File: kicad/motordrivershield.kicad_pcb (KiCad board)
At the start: 2 copper layers, 100 x 60 mm, 142 parts, among them CN1 ARDUINO_MKR, CN2 QWIIC, P1 CONN_01X03, P2 CONN_01X03, P5 WR-TBL_691313710002, P6 WR-TBL_691313710002, P7 CONN_01X02, P8 WR-TBL_691313710002, Q1 2N7002, U1 PCA9685_TSSOP28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

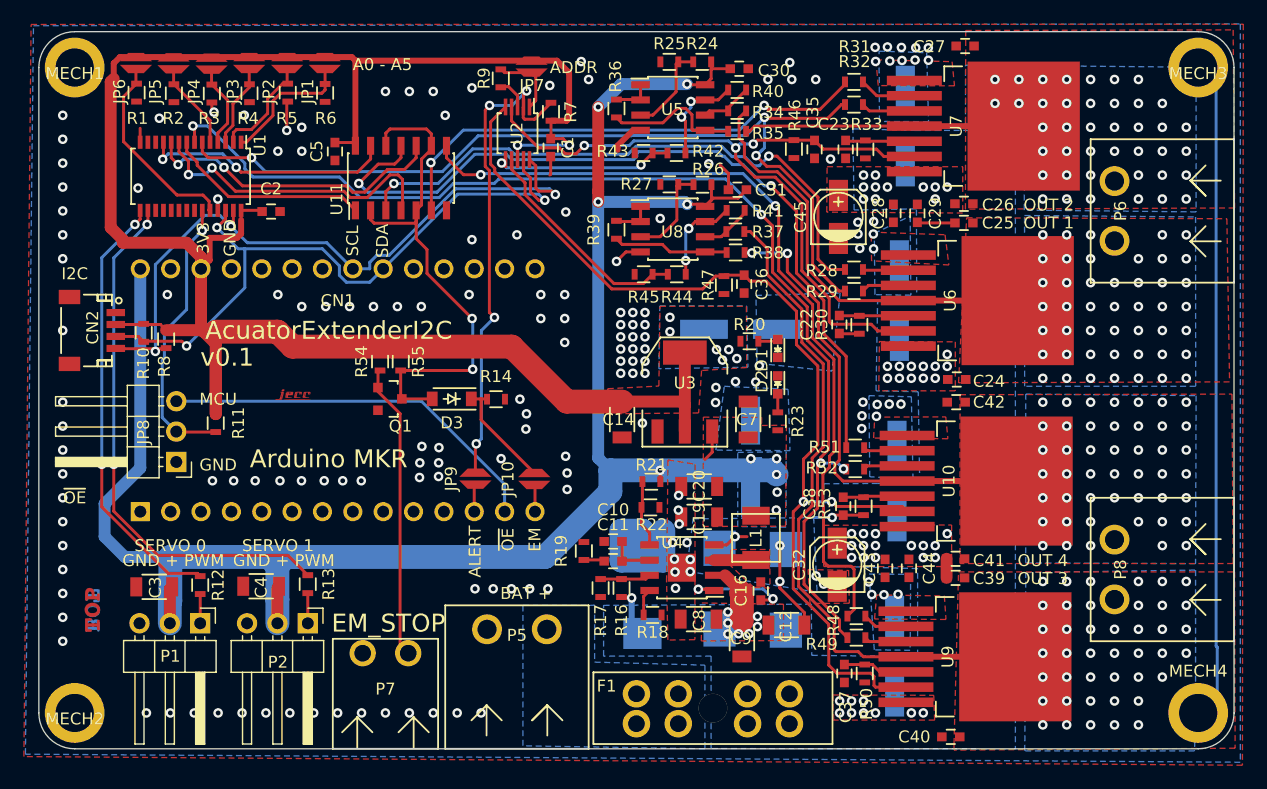
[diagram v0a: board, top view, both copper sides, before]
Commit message: added nano footprint
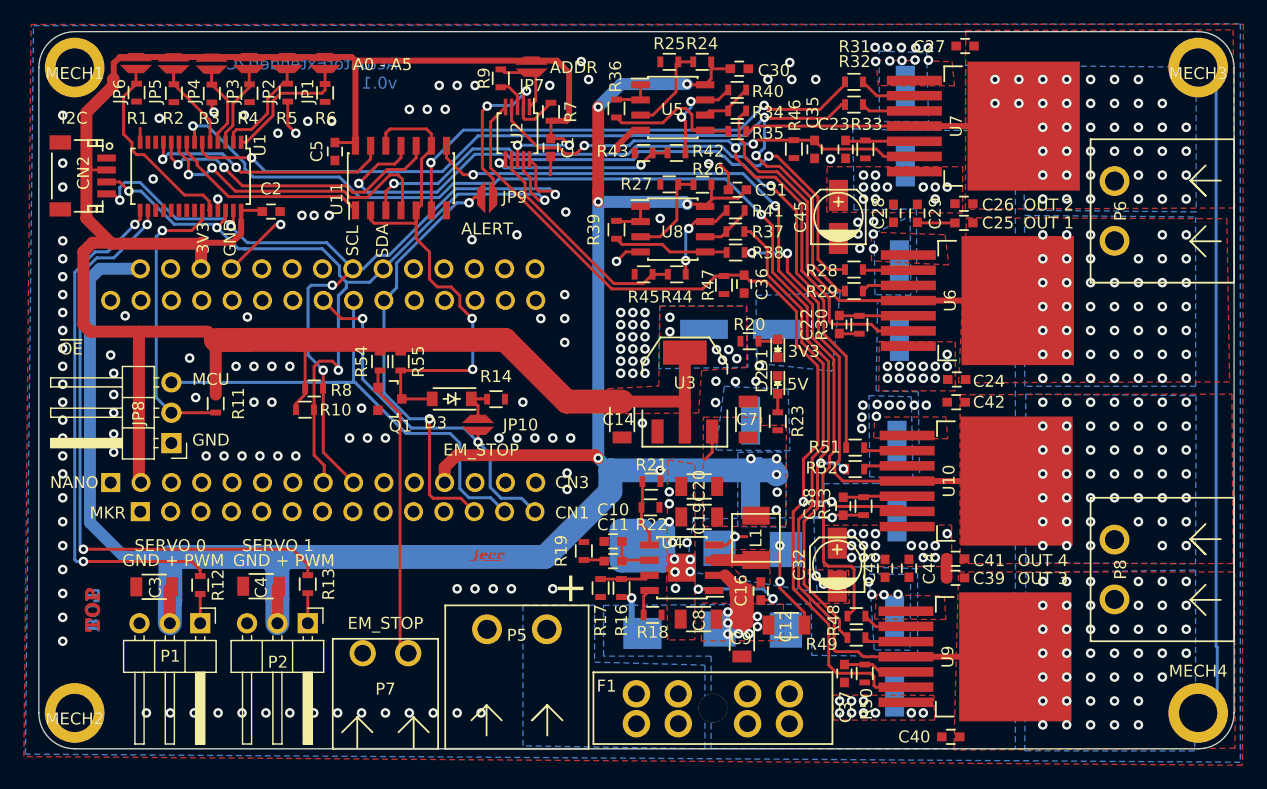
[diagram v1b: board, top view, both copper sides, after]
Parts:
- added CN3: ARDUINO_NANO_33, MODULE_compute:ARDUINO_NANO_33, F.Cu at (113.8, 70.1)
- moved JP9 23.6 mm to (127.5, 53.8), turned to 0 degrees
- moved L2 21.1 mm to (127.5, 83.8)
- moved R10 14.9 mm to (112.3, 71.6), turned to 0 degrees
- moved R8 13.0 mm to (113.0, 69.8), turned to 0 degrees
- moved CN2 13.0 mm to (93.7, 52.1)
- moved JP10 6.53 mm to (126.7, 72.9)
- moved R11 1.63 mm to (104.8, 71.1)
- moved JP8 1.63 mm to (101.1, 74.4)
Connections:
- net Net-(CN1-Pad12) renamed /AL_MCU
- net Net-(CN1-Pad14) renamed /EM_MCU
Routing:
- net /AL_MCU: track 2.54 -> 36.1 mm, vias 0 -> 2
- net /EM_MCU: track 2.26 -> 30.6 mm, vias 0 -> 2
- net /ALERT: track 40.9 -> 17.3 mm, vias 4 -> 2
- net +3V3: track 170.3 -> 192.5 mm
- net +5V: track 181.7 -> 199.4 mm, vias 10 -> 11
- net /SCL: track 58.0 -> 73.1 mm, vias 3 -> 5
- net /SDA: track 55.7 -> 70.5 mm, vias 3 -> 4
- net /~OE_MCU: track 32.6 -> 43.0 mm
- net Net-(R13-Pad2): track 44.8 -> 51.9 mm
- net Net-(R12-Pad2): track 36.8 -> 43.5 mm
- net EM_STOP: track 9.38 -> 3.23 mm
- net GND: track 104.0 -> 110.2 mm, vias 169 -> 184
- net /powertrain/EM_S: track 44.6 -> 45.3 mm
- net /~OE: track 23.7 -> 24.2 mm
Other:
- board text added: "+"
- board text added: "5V"
- board text added: "ActuatorExtenderI2C v0.1"
- board text added: "MKR"
- board text added: "NANO"
- board text removed: "AcuatorExtenderI2C"
- board text removed: "Arduino MKR"
- board text removed: "BAT +"
- board text removed: "v0.1"

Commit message: changed 5V power rail
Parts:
- moved C9 3.74 mm to (145.2, 91.7), turned to 180 degrees
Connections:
- CN1 pad 27: (no net) -> +5V
- CN1 pad 28: +5V -> (no net)
- CN3 pad 12: +5V -> (no net)
- CN3 pad 15: (no net) -> +5V
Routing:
- net GND: track 110.2 -> 117.7 mm, vias 184 -> 195
- net +5V: track 199.4 -> 197.8 mm
- net /SCL: track 73.1 -> 74.0 mm
- net +3V3: track 192.5 -> 191.8 mm

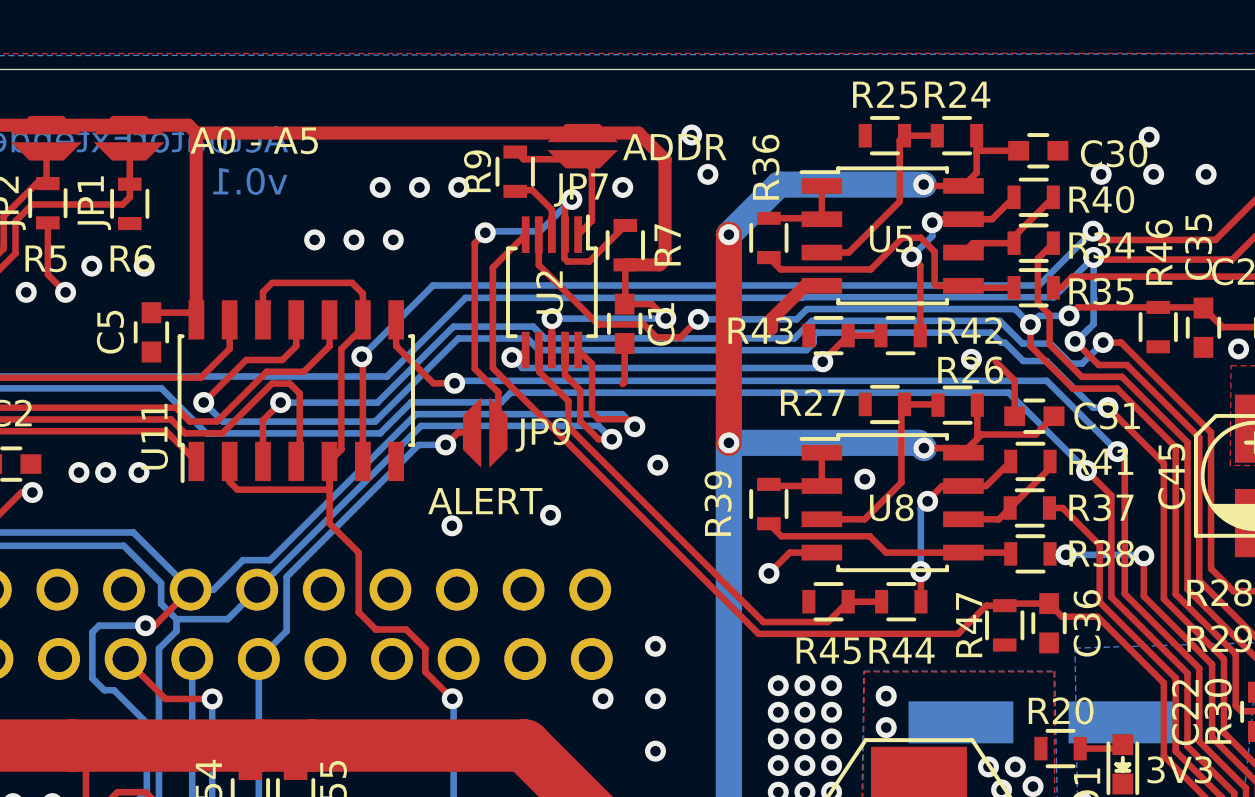
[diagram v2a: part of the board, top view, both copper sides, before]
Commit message: added capacitors
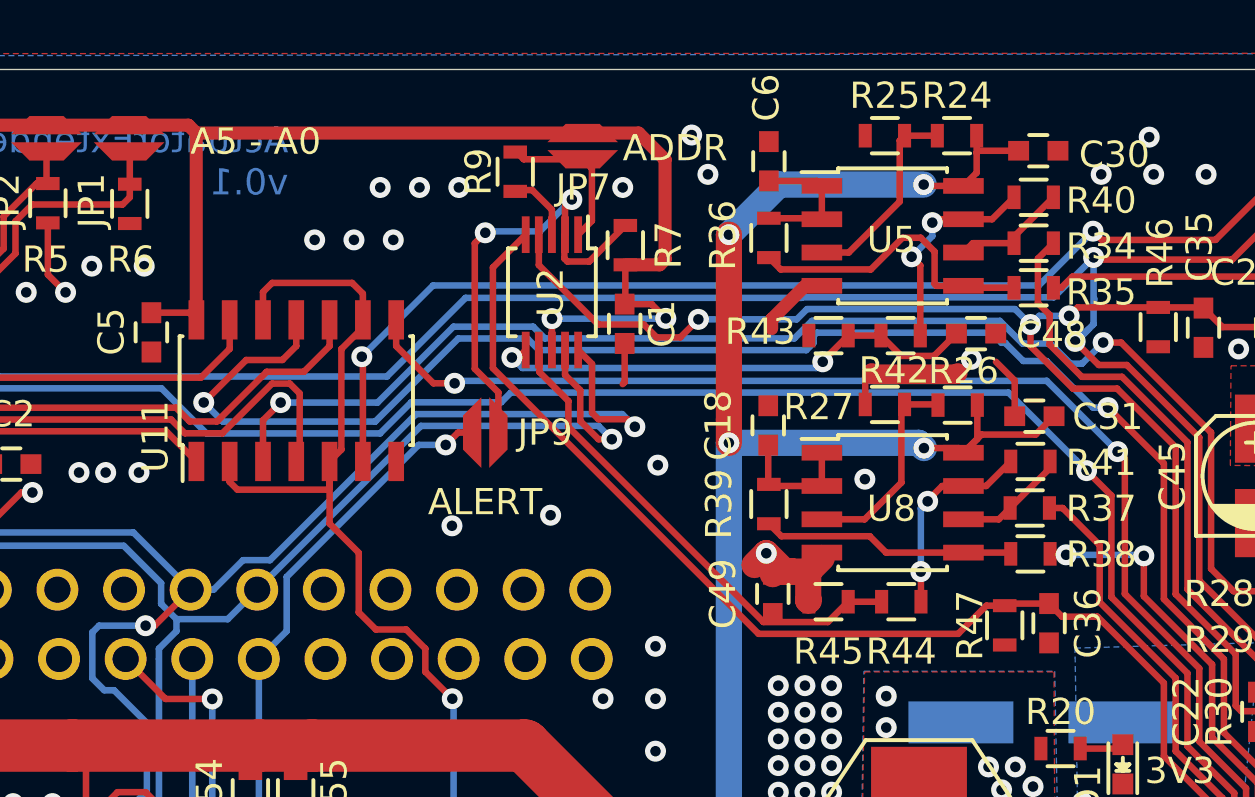
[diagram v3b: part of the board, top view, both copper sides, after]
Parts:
- added C18: 100nF, capacitors:C_0603, F.Cu at (138.3, 53.6)
- added C48: 100nF, capacitors:C_0603, F.Cu at (146.2, 50.1)
- added C49: 100nF, capacitors:C_0603, F.Cu at (138.5, 60.0)
- added C6: 100nF, capacitors:C_0603, F.Cu at (138.3, 43.5)
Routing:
- net GND: track 117.7 -> 126.5 mm
- net BEMF12: track 15.4 -> 19.0 mm
- net Net-(C6-Pad1): track 3.31 -> 5.41 mm
- net Net-(C18-Pad1): track 3.32 -> 4.83 mm
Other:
- board text added: "A5 - A0"
- board text removed: "A0 - A5"

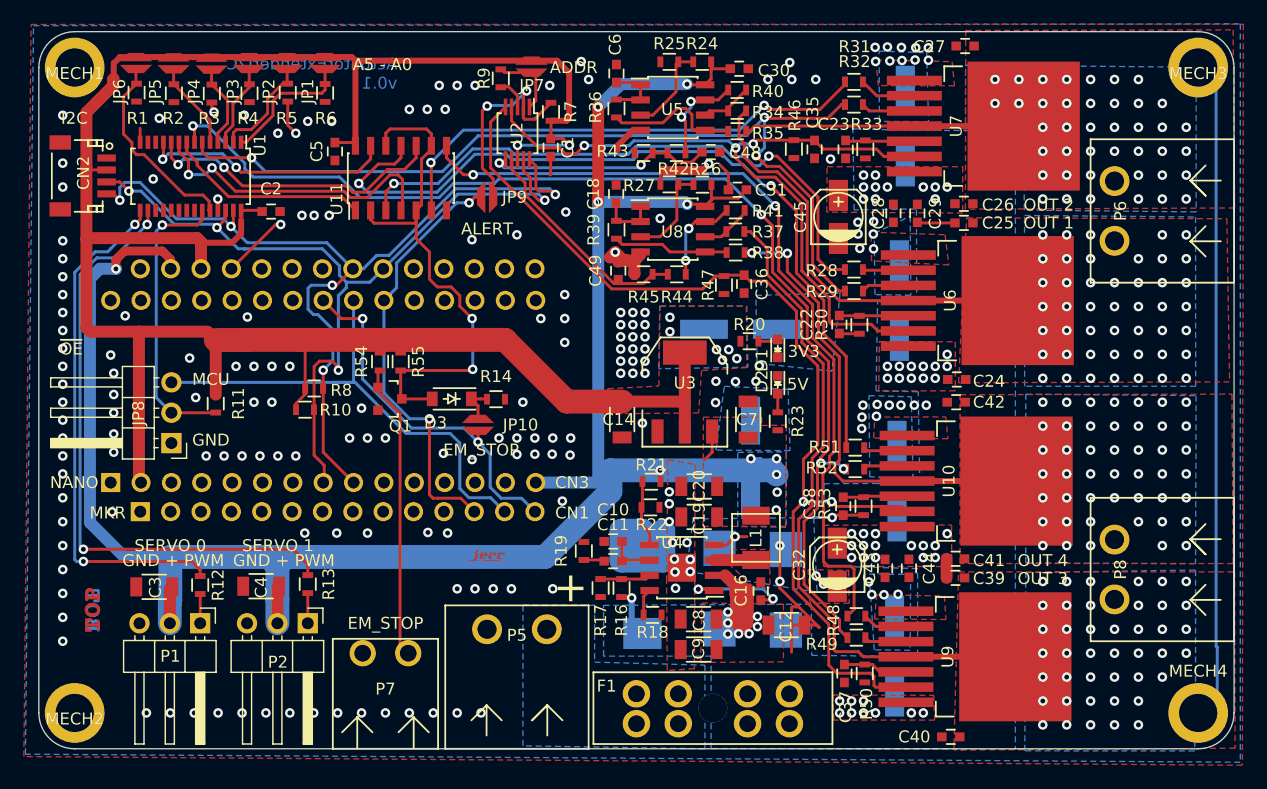
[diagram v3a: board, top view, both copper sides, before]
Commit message: added leds, updated capacitor values and changed silkscreen
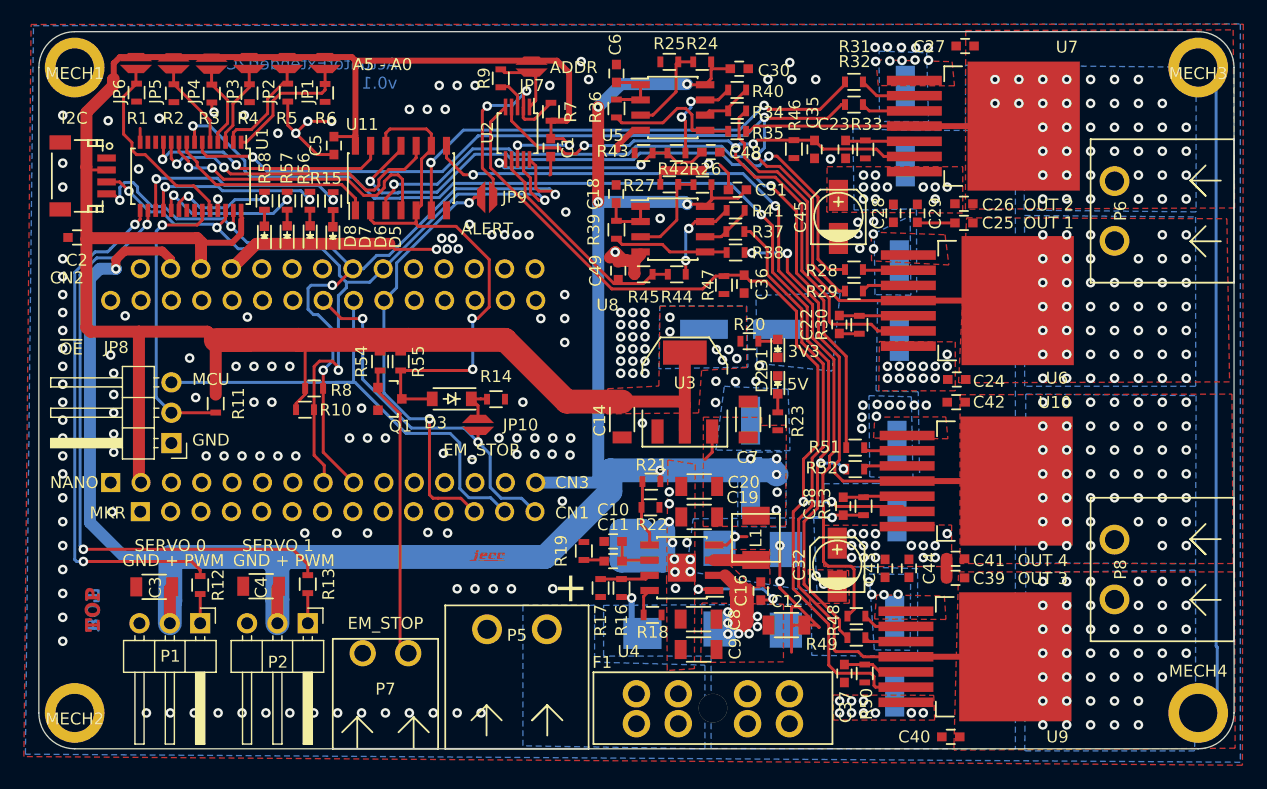
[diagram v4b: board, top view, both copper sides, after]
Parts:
- added D5: Led_Small, LEDs:LED_0603, F.Cu at (114.6, 57.1)
- added D6: Led_Small, LEDs:LED_0603, F.Cu at (112.7, 57.0)
- added D7: Led_Small, LEDs:LED_0603, F.Cu at (110.8, 57.0)
- added D8: Led_Small, LEDs:LED_0603, F.Cu at (108.9, 57.0)
- added R15: 1k, resistors:R_0603, F.Cu at (114.6, 54.2)
- added R56: 1k, resistors:R_0603, F.Cu at (112.7, 54.1)
- added R57: 1k, resistors:R_0603, F.Cu at (110.8, 54.1)
- added R58: 1k, resistors:R_0603, F.Cu at (108.9, 54.1)
- C48, C49: value 100nF -> 1nF
- moved C2 16.4 mm to (93.2, 57.2), turned to 180 degrees
- moved C5 0.50 mm to (114.7, 49.5)
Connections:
- U1 pad 17: (no net) -> Net-(R15-Pad2)
- U1 pad 18: (no net) -> Net-(R56-Pad2)
- U1 pad 19: (no net) -> Net-(R57-Pad2)
- U1 pad 20: (no net) -> Net-(R58-Pad2)
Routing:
- net GND: track 126.5 -> 146.4 mm, vias 195 -> 199
- net Net-(R15-Pad2): track 0.00 -> 18.9 mm, vias 0 -> 2
- net Net-(R56-Pad2): track 0.00 -> 15.2 mm, vias 0 -> 2
- net Net-(R57-Pad2): track 0.00 -> 12.6 mm, vias 0 -> 2
- net Net-(R58-Pad2): track 0.00 -> 9.33 mm, vias 0 -> 2
- net /powertrain/IN4: track 67.8 -> 65.4 mm
- net +3V3: track 191.8 -> 190.1 mm
- net /powertrain/EM_S: track 45.3 -> 46.9 mm
- net Net-(D5-Pad2): track 0.00 -> 1.41 mm
- net Net-(D8-Pad2): track 0.00 -> 1.38 mm
- net Net-(D6-Pad2): track 0.00 -> 1.36 mm
- net Net-(D7-Pad2): track 0.00 -> 1.35 mm
- net PWM2: track 25.8 -> 25.1 mm
- net PWM1: track 17.1 -> 17.7 mm
